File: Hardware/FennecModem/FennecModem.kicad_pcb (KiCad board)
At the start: 2 copper layers, 75 x 116.7 mm, 43 parts, among them J101 USB_C_Receptacle_USB2.0, J102 ICSP, J201 Conn_Coaxial, SW101 RESET, U101 ATmega32U4-A, U201 DRA818V, U301 NCP1117-12_SOT223, Y101 16mHz

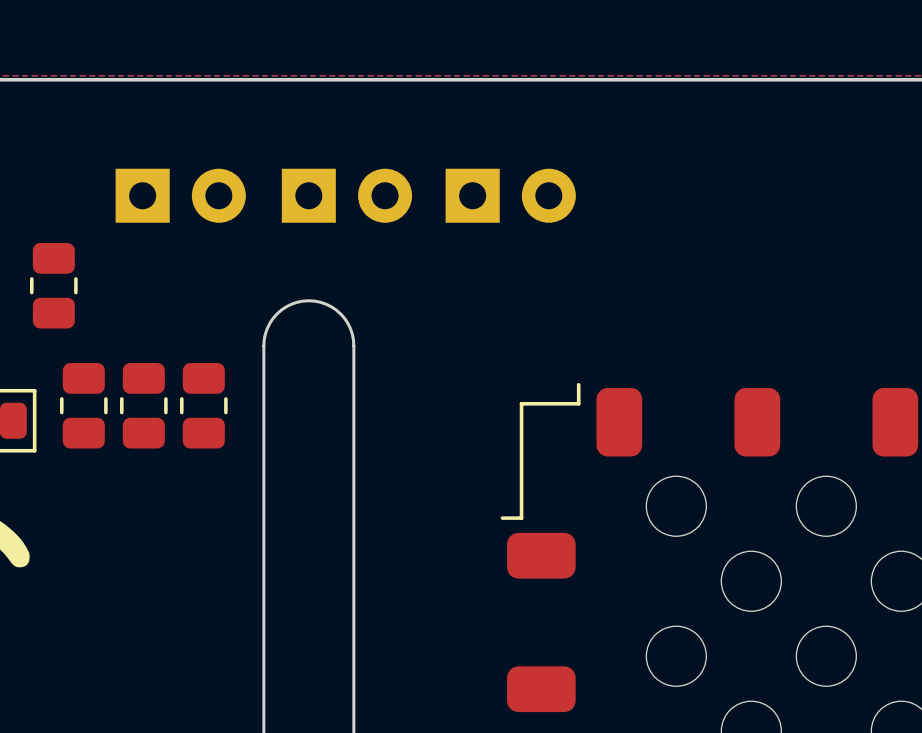
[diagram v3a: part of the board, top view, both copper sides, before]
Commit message: Bump rails and add PWR LED
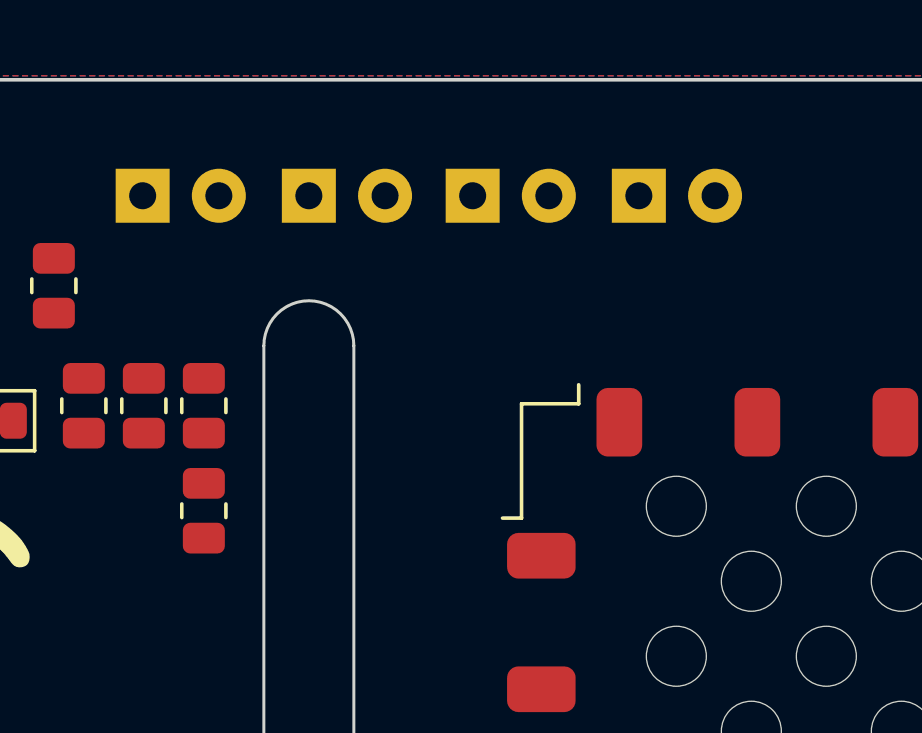
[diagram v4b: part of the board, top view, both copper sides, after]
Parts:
- added D104: PWR, LED_THT:LED_D3.0mm_Horizontal_O1.27mm_Z2.0mm, B.Cu at (154.5, 44.0)
- added R108: 330, Resistor_SMD:R_0805_2012Metric, F.Cu at (140.0, 54.5)
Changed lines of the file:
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@@
   (net 71 "/Backplane/CARD_SEL")
   (net 72 "/Backplane/I2C_SCL")
+  (net 73 "Net-(D104-A)")
   (footprint "Capacitor_SMD:C_0805_2012Metric" (layer "F.Cu")
     (at 166.6575 114.06)
@@
     )
   )
+  (footprint "Resistor_SMD:R_0805_2012Metric" (layer "F.Cu")
+    (at 140 54.5 90)
+    (descr "Resistor SMD 0805 (2012 Metric), square (rectangular) end terminal, IPC_7351 nominal, (Body size source: IPC-SM-782 page 72, https://www.pcb-3d.com/wordpress/wp-content/uploads/ipc-sm-782a_amendment_1_and_2.pdf), generated with kicad-footprint-generator")
+    (tags "resistor")
+    (property "Sheetfile" "FennecModem.kicad_sch")
+    (property "Sheetname" "")
+    (property "ki_description" "Resistor")
+    (property "ki_keywords" "R res resistor")
+    (attr smd)
+    (fp_text reference "R108" (at 0 -1.65 90) (layer "F.SilkS") hide
+        (effects (font (size 1 1) (thickness 0.15)))
+    )
+    (fp_text value "330" (at 0 1.65 90) (layer "F.Fab")
+        (effects (font (size 1 1) (thickness 0.15)))
+    )
+    (fp_text user "${REFERENCE}" (at 0 0 90) (layer "F.Fab")
+        (effects (font (size 0.5 0.5) (thickness 0.08)))
+    )
+    (fp_line (start -0.227064 -0.735) (end 0.227064 -0.735)
+      (stroke (width 0.12) (type solid)) (layer "F.SilkS"))
+    (fp_line (start -0.227064 0.735) (end 0.227064 0.735)
+      (stroke (width 0.12) (type solid)) (layer "F.SilkS"))
+    (fp_line (start -1.68 -0.95) (end 1.68 -0.95)
+      (stroke (width 0.05) (type solid)) (layer "F.CrtYd"))
+    (fp_line (start -1.68 0.95) (end -1.68 -0.95)
+      (stroke (width 0.05) (type solid)) (layer "F.CrtYd"))
+    (fp_line (start 1.68 -0.95) (end 1.68 0.95)
+      (stroke (width 0.05) (type solid)) (layer "F.CrtYd"))
+    (fp_line (start 1.68 0.95) (end -1.68 0.95)
+      (stroke (width 0.05) (type solid)) (layer "F.CrtYd"))
+    (fp_line (start -1 -0.625) (end 1 -0.625)
+      (stroke (width 0.1) (type solid)) (layer "F.Fab"))
+    (fp_line (start -1 0.625) (end -1 -0.625)
+      (stroke (width 0.1) (type solid)) (layer "F.Fab"))
+    (fp_line (start 1 -0.625) (end 1 0.625)
+      (stroke (width 0.1) (type solid)) (layer "F.Fab"))
+    (fp_line (start 1 0.625) (end -1 0.625)
+      (stroke (width 0.1) (type solid)) (layer "F.Fab"))
+    (pad "1" smd roundrect (at -0.9125 0 90) (size 1.025 1.4) (layers "F.Cu" "F.Paste" "F.Mask") (roundrect_rratio 0.243902)
+      (net 73 "Net-(D104-A)") (pintype "passive"))
+    (pad "2" smd roundrect (at 0.9125 0 90) (size 1.025 1.4) (layers "F.Cu" "F.Paste" "F.Mask") (roundrect_rratio 0.243902)
+      (net 2 "+5V") (pintype "passive"))
+    (model "${KICAD6_3DMODEL_DIR}/Resistor_SMD.3dshapes/R_0805_2012Metric.wrl"
+      (offset (xyz 0 0 0))
+      (scale (xyz 1 1 1))
+      (rotate (xyz 0 0 0))
+    )
+  )
   (footprint "Crystal:Crystal_SMD_HC49-SD" (layer "F.Cu")
     (at 140 137 -45)
@@
     )
   )
+  (footprint "LED_THT:LED_D3.0mm_Horizontal_O1.27mm_Z2.0mm" (layer "B.Cu")
+    (at 154.5 44)
+    (descr "LED, diameter 3.0mm z-position of LED center 2.0mm, 2 pins")
+    (tags "LED diameter 3.0mm z-position of LED center 2.0mm 2 pins")
+    (property "Sheetfile" "FennecModem.kicad_sch")
+    (property "Sheetname" "")
+    (property "ki_description" "Light emitting diode")
+    (property "ki_keywords" "LED diode")
+    (attr through_hole)
+    (fp_text reference "D104" (at 1.27 1.96) (layer "B.SilkS") hide
+        (effects (font (size 1 1) (thickness 0.15)) (justify mirror))
+    )
+    (fp_text value "PWR" (at 1.27 -3) (layer "B.SilkS")
+        (effects (font (size 1 1) (thickness 0.15)) (justify mirror))
+    )
+    (fp_line (start -0.29 -1.21) (end -0.29 -5.07)
+      (stroke (width 0.12) (type solid)) (layer "B.SilkS"))
+    (fp_line (start -0.29 -1.21) (end 2.83 -1.21)
+      (stroke (width 0.12) (type solid)) (layer "B.SilkS"))
+    (fp_line (start 0 -1.21) (end 0 -1.21)
+      (stroke (width 0.12) (type solid)) (layer "B.SilkS"))
+    (fp_line (start 0 -1.21) (end 0 -1.08)
+      (stroke (width 0.12) (type solid)) (layer "B.SilkS"))
+    (fp_line (start 0 -1.08) (end 0 -1.21)
+      (stroke (width 0.12) (type solid)) (layer "B.SilkS"))
+    (fp_line (start 0 -1.08) (end 0 -1.08)
+      (stroke (width 0.12) (type solid)) (layer "B.SilkS"))
+    (fp_line (start 2.54 -1.21) (end 2.54 -1.21)
+      (stroke (width 0.12) (type solid)) (layer "B.SilkS"))
+    (fp_line (start 2.54 -1.21) (end 2.54 -1.08)
+      (stroke (width 0.12) (type solid)) (layer "B.SilkS"))
+    (fp_line (start 2.54 -1.08) (end 2.54 -1.21)
+      (stroke (width 0.12) (type solid)) (layer "B.SilkS"))
+    (fp_line (start 2.54 -1.08) (end 2.54 -1.08)
+      (stroke (width 0.12) (type solid)) (layer "B.SilkS"))
+    (fp_line (start 2.83 -2.33) (end 2.83 -1.21)
+      (stroke (width 0.12) (type solid)) (layer "B.SilkS"))
+    (fp_line (start 2.83 -1.21) (end 2.83 -5.07)
+      (stroke (width 0.12) (type solid)) (layer "B.SilkS"))
+    (fp_line (start 2.83 -1.21) (end 3.23 -1.21)
+      (stroke (width 0.12) (type solid)) (layer "B.SilkS"))
+    (fp_line (start 3.23 -2.33) (end 2.83 -2.33)
+      (stroke (width 0.12) (type solid)) (layer "B.SilkS"))
+    (fp_line (start 3.23 -1.21) (end 3.23 -2.33)
+      (stroke (width 0.12) (type solid)) (layer "B.SilkS"))
+    (fp_arc (start -0.29 -5.07) (mid 1.27 -6.63) (end 2.83 -5.07)
+      (stroke (width 0.12) (type solid)) (layer "B.SilkS"))
+    (fp_line (start -1.25 -6.9) (end 3.75 -6.9)
+      (stroke (width 0.05) (type solid)) (layer "B.CrtYd"))
+    (fp_line (start -1.25 1.25) (end -1.25 -6.9)
+      (stroke (width 0.05) (type solid)) (layer "B.CrtYd"))
+    (fp_line (start 3.75 -6.9) (end 3.75 1.25)
+      (stroke (width 0.05) (type solid)) (layer "B.CrtYd"))
+    (fp_line (start 3.75 1.25) (end -1.25 1.25)
+      (stroke (width 0.05) (type solid)) (layer "B.CrtYd"))
+    (fp_line (start -0.23 -1.27) (end -0.23 -5.07)
+      (stroke (width 0.1) (type solid)) (layer "B.Fab"))
+    (fp_line (start -0.23 -1.27) (end 2.77 -1.27)
+      (stroke (width 0.1) (type solid)) (layer "B.Fab"))
+    (fp_line (start 0 -1.27) (end 0 -1.27)
+      (stroke (width 0.1) (type solid)) (layer "B.Fab"))
+    (fp_line (start 0 -1.27) (end 0 0)
+      (stroke (width 0.1) (type solid)) (layer "B.Fab"))
+    (fp_line (start 0 0) (end 0 -1.27)
+      (stroke (width 0.1) (type solid)) (layer "B.Fab"))
+    (fp_line (start 0 0) (end 0 0)
+      (stroke (width 0.1) (type solid)) (layer "B.Fab"))
+    (fp_line (start 2.54 -1.27) (end 2.54 -1.27)
+      (stroke (width 0.1) (type solid)) (layer "B.Fab"))
+    (fp_line (start 2.54 -1.27) (end 2.54 0)
+      (stroke (width 0.1) (type solid)) (layer "B.Fab"))
+    (fp_line (start 2.54 0) (end 2.54 -1.27)
+      (stroke (width 0.1) (type solid)) (layer "B.Fab"))
+    (fp_line (start 2.54 0) (end 2.54 0)
+      (stroke (width 0.1) (type solid)) (layer "B.Fab"))
+    (fp_line (start 2.77 -2.27) (end 2.77 -1.27)
+      (stroke (width 0.1) (type solid)) (layer "B.Fab"))
+    (fp_line (start 2.77 -1.27) (end 2.77 -5.07)
+      (stroke (width 0.1) (type solid)) (layer "B.Fab"))
+    (fp_line (start 2.77 -1.27) (end 3.17 -1.27)
+      (stroke (width 0.1) (type solid)) (layer "B.Fab"))
+    (fp_line (start 3.17 -2.27) (end 2.77 -2.27)
+      (stroke (width 0.1) (type solid)) (layer "B.Fab"))
+    (fp_line (start 3.17 -1.27) (end 3.17 -2.27)
+      (stroke (width 0.1) (type solid)) (layer "B.Fab"))
+    (fp_arc (start -0.23 -5.07) (mid 1.27 -6.57) (end 2.77 -5.07)
+      (stroke (width 0.1) (type solid)) (layer "B.Fab"))
+    (pad "1" thru_hole rect (at 0 0) (size 1.8 1.8) (drill 0.9) (layers "*.Cu" "*.Mask")
+      (net 3 "GND") (pinfunction "K") (pintype "passive"))
+    (pad "2" thru_hole circle (at 2.54 0) (size 1.8 1.8) (drill 0.9) (layers "*.Cu" "*.Mask")
+      (net 73 "Net-(D104-A)") (pinfunction "A") (pintype "passive"))
+    (model "${KICAD6_3DMODEL_DIR}/LED_THT.3dshapes/LED_D3.0mm_Horizontal_O1.27mm_Z2.0mm.wrl"
+      (offset (xyz 0 0 0))
+      (scale (xyz 1 1 1))
+      (rotate (xyz 0 0 0))
+    )
+  )

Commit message: Bump backplane
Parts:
- moved R206 64.5 mm to (147.4, 65.0)
- moved R201 7.95 mm to (175.6, 115.5)
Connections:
- D202 pad 1: /Radio/RXD -> /TXD
- D204 pad 1: /Radio/TXD -> /RXD
- U101 pad 18: unconnected-(U101-PD0-Pad18) -> /I2C_CLK
- U101 pad 19: unconnected-(U101-PD1-Pad19) -> /I2C_SDA
- U101 pad 20: unconnected-(U101-PD2-Pad20) -> /RXD
- U101 pad 21: unconnected-(U101-PD3-Pad21) -> /TXD
- U101 pad 30: unconnected-(U101-PB6-Pad30) -> /TX_SIGNAL
- U101 pad 41: unconnected-(U101-PF0-Pad41) -> /RX_SIGNAL
- U201 pad 16: /Radio/RXD -> /TXD
- U201 pad 17: /Radio/TXD -> /RXD
- U302 pad 10: (no net) -> unconnected-(U302-CARD_SEL4-Pad10)
- U302 pad 12: (no net) -> /Backplane/SPI_CLK
- U302 pad 14: (no net) -> /Backplane/SPI_SDA1
- U302 pad 16: (no net) -> /Backplane/SPI_SDA2
- U302 pad 17: (no net) -> unconnected-(U302-SPI_SD0-Pad17)
- U302 pad 18: (no net) -> /Backplane/SPI_SDA3
- U302 pad 20: (no net) -> /Backplane/SPI_SDA4
- U302 pad 5: (no net) -> unconnected-(U302-CARD_EN2-Pad5)
- U302 pad 6: (no net) -> unconnected-(U302-CARD_SEL2-Pad6)
- U302 pad 7: (no net) -> unconnected-(U302-CARD_EN3-Pad7)
- U302 pad 8: (no net) -> unconnected-(U302-CARD_SEL3-Pad8)
- U302 pad 9: (no net) -> unconnected-(U302-CARD_EN4-Pad9)

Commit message: Bump everything with new backplane design
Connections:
- U302 pad 19: (no net) -> unconnected-(U302-GPIO1-Pad19)
- U302 pad 21: (no net) -> unconnected-(U302-GPIO2-Pad21)
- U302 pad 22: (no net) -> unconnected-(U302-GPIO3-Pad22)
- U302 pad 23: (no net) -> unconnected-(U302-UNUSED1-Pad23)
- U302 pad 24: (no net) -> unconnected-(U302-UNUSED2-Pad24)
- U302 pad 25: (no net) -> unconnected-(U302-UNUSED3-Pad25)
- U302 pad 26: (no net) -> unconnected-(U302-UNUSED4-Pad26)
- U302 pad 27: (no net) -> unconnected-(U302-CANH-Pad27)
- U302 pad 28: (no net) -> unconnected-(U302-CANL-Pad28)
- U302 pad 29: (no net) -> unconnected-(U302-UNUSED5-Pad29)
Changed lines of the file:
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@@
   (net 82 "/Backplane/SPI_SDA3")
   (net 83 "/Backplane/SPI_SDA4")
+  (net 84 "unconnected-(U302-GPIO1-Pad19)")
+  (net 85 "unconnected-(U302-GPIO2-Pad21)")
+  (net 86 "unconnected-(U302-GPIO3-Pad22)")
+  (net 87 "unconnected-(U302-UNUSED1-Pad23)")
+  (net 88 "unconnected-(U302-UNUSED2-Pad24)")
+  (net 89 "unconnected-(U302-UNUSED3-Pad25)")
+  (net 90 "unconnected-(U302-UNUSED4-Pad26)")
+  (net 91 "unconnected-(U302-CANH-Pad27)")
+  (net 92 "unconnected-(U302-CANL-Pad28)")
+  (net 93 "unconnected-(U302-UNUSED5-Pad29)")
   (footprint "Capacitor_SMD:C_0805_2012Metric" (layer "F.Cu")
     (at 166.6575 114.06)
@@
       (net 82 "/Backplane/SPI_SDA3") (pinfunction "SPI_SDA3") (pintype "unspecified"))
     (pad "19" connect roundrect (at 7.92 4 90) (size 5 2) (layers "F.Cu" "F.Mask") (roundrect_rratio 0)
-      (chamfer_ratio 0.2) (chamfer top_left bottom_left))
+      (chamfer_ratio 0.2) (chamfer top_left bottom_left)
+      (net 84 "unconnected-(U302-GPIO1-Pad19)") (pinfunction "GPIO1") (pintype "unspecified+no_connect"))
     (pad "20" connect roundrect (at 7.92 4 270) (size 5 2) (layers "B.Cu" "B.Mask") (roundrect_rratio 0)
       (chamfer_ratio 0.2) (chamfer top_right bottom_right)
       (net 83 "/Backplane/SPI_SDA4") (pinfunction "SPI_SDA4") (pintype "unspecified"))
     (pad "21" connect roundrect (at 11.88 4 90) (size 5 2) (layers "F.Cu" "F.Mask") (roundrect_rratio 0)
-      (chamfer_ratio 0.2) (chamfer top_left bottom_left))
+      (chamfer_ratio 0.2) (chamfer top_left bottom_left)
+      (net 85 "unconnected-(U302-GPIO2-Pad21)") (pinfunction "GPIO2") (pintype "unspecified+no_connect"))
     (pad "22" connect roundrect (at 11.88 4 270) (size 5 2) (layers "B.Cu" "B.Mask") (roundrect_rratio 0)
-      (chamfer_ratio 0.2) (chamfer top_right bottom_right))
+      (chamfer_ratio 0.2) (chamfer top_right bottom_right)
+      (net 86 "unconnected-(U302-GPIO3-Pad22)") (pinfunction "GPIO3") (pintype "unspecified+no_connect"))
     (pad "23" connect roundrect (at 15.84 4 90) (size 5 2) (layers "F.Cu" "F.Mask") (roundrect_rratio 0)
-      (chamfer_ratio 0.2) (chamfer top_left bottom_left))
+      (chamfer_ratio 0.2) (chamfer top_left bottom_left)
+      (net 87 "unconnected-(U302-UNUSED1-Pad23)") (pinfunction "UNUSED1") (pintype "no_connect"))
     (pad "24" connect roundrect (at 15.84 4 270) (size 5 2) (layers "B.Cu" "B.Mask") (roundrect_rratio 0)
-      (chamfer_ratio 0.2) (chamfer top_right bottom_right))
+      (chamfer_ratio 0.2) (chamfer top_right bottom_right)
+      (net 88 "unconnected-(U302-UNUSED2-Pad24)") (pinfunction "UNUSED2") (pintype "no_connect"))
     (pad "25" connect roundrect (at 19.8 4 90) (size 5 2) (layers "F.Cu" "F.Mask") (roundrect_rratio 0)
-      (chamfer_ratio 0.2) (chamfer top_left bottom_left))
+      (chamfer_ratio 0.2) (chamfer top_left bottom_left)
+      (net 89 "unconnected-(U302-UNUSED3-Pad25)") (pinfunction "UNUSED3") (pintype "no_connect"))
     (pad "26" connect roundrect (at 19.8 4 270) (size 5 2) (layers "B.Cu" "B.Mask") (roundrect_rratio 0)
-      (chamfer_ratio 0.2) (chamfer top_right bottom_right))
+      (chamfer_ratio 0.2) (chamfer top_right bottom_right)
+      (net 90 "unconnected-(U302-UNUSED4-Pad26)") (pinfunction "UNUSED4") (pintype "no_connect"))
     (pad "27" connect roundrect (at 23.76 4 90) (size 5 2) (layers "F.Cu" "F.Mask") (roundrect_rratio 0)
-      (chamfer_ratio 0.2) (chamfer top_left bottom_left))
+      (chamfer_ratio 0.2) (chamfer top_left bottom_left)
+      (net 91 "unconnected-(U302-CANH-Pad27)") (pinfunction "CANH") (pintype "unspecified+no_connect"))
     (pad "28" connect roundrect (at 23.76 4 270) (size 5 2) (layers "B.Cu" "B.Mask") (roundrect_rratio 0)
-      (chamfer_ratio 0.2) (chamfer top_right bottom_right))
+      (chamfer_ratio 0.2) (chamfer top_right bottom_right)
+      (net 92 "unconnected-(U302-CANL-Pad28)") (pinfunction "CANL") (pintype "unspecified+no_connect"))
     (pad "29" connect roundrect (at 27.72 4 90) (size 5 2) (layers "F.Cu" "F.Mask") (roundrect_rratio 0)
-      (chamfer_ratio 0.2) (chamfer top_left bottom_left))
+      (chamfer_ratio 0.2) (chamfer top_left bottom_left)
+      (net 93 "unconnected-(U302-UNUSED5-Pad29)") (pinfunction "UNUSED5") (pintype "no_connect"))
     (pad "30" connect roundrect (at 27.72 4 270) (size 5 2) (layers "B.Cu" "B.Mask") (roundrect_rratio 0)
       (chamfer_ratio 0.2) (chamfer top_right bottom_right)

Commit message: Add all
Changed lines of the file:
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@@
     (effects (font (size 1 1) (thickness 0.15)))
   )
-  (gr_text "${FULL_REVISION}" (at 125 84.25) (layer "F.SilkS")
+  (gr_text "${FULL_REVISION}" (at 125 85.5) (layer "F.SilkS")
     (effects (font (size 1.5 1.5) (thickness 0.3) bold) (justify top))
   )

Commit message: Begin laying out and prepping for new tests
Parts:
- added D105: PRTR5V0U2X, Package_TO_SOT_SMD:SOT-143, F.Cu at (123.0, 50.5)
- added J202: PTT_AMP, Connector_JST:JST_XH_S2B-XH-A-1_1x02_P2.50mm_Horizontal, F.Cu at (161.5, 44.9)
- added R207: ?k, Resistor_SMD:R_0805_2012Metric, F.Cu at (143.2, 62.8)
- added U202: PC817, Package_DIP:DIP-4_W7.62mm_SMDSocket_SmallPads, F.Cu at (143.5, 56.2)
- moved R108 15.6 mm to (153.3, 46.5), turned to 180 degrees
- moved R103 9.18 mm to (148.0, 46.5), turned to 180 degrees
- moved R202 6.30 mm to (142.4, 46.5), turned to 180 degrees
- moved R205 5.27 mm to (138.8, 46.5), turned to 0 degrees
- moved D101 2.71 mm to (146.2, 44.0)
- moved D104 2.71 mm to (151.8, 44.0)
- moved D201 2.71 mm to (140.8, 44.0)
- moved D203 2.71 mm to (135.2, 44.0)
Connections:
- D103 pad 1: +5V -> unconnected-(D103-K-Pad1)
